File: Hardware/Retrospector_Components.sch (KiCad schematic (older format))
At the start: 134 parts, among them J1 SWD_Header, J2 Eurorack_10_pin_power, J3 Conn_01x08_Male, J4 Conn_01x08_Male, J5 Conn_01x08_Male, J6 Conn_01x08_Male, J7 USB_B_Micro, U1 STM32H743ZITx, U2 IS42S16800F-7TLI, U3 PCM5100APW, U4 SSI2164, U5 MCP6004, U6 MCP6004, U7 TL074, U8 NCV1117DT33T5G, U9 BA7807FP-E2, Y1 8MHz 20pF

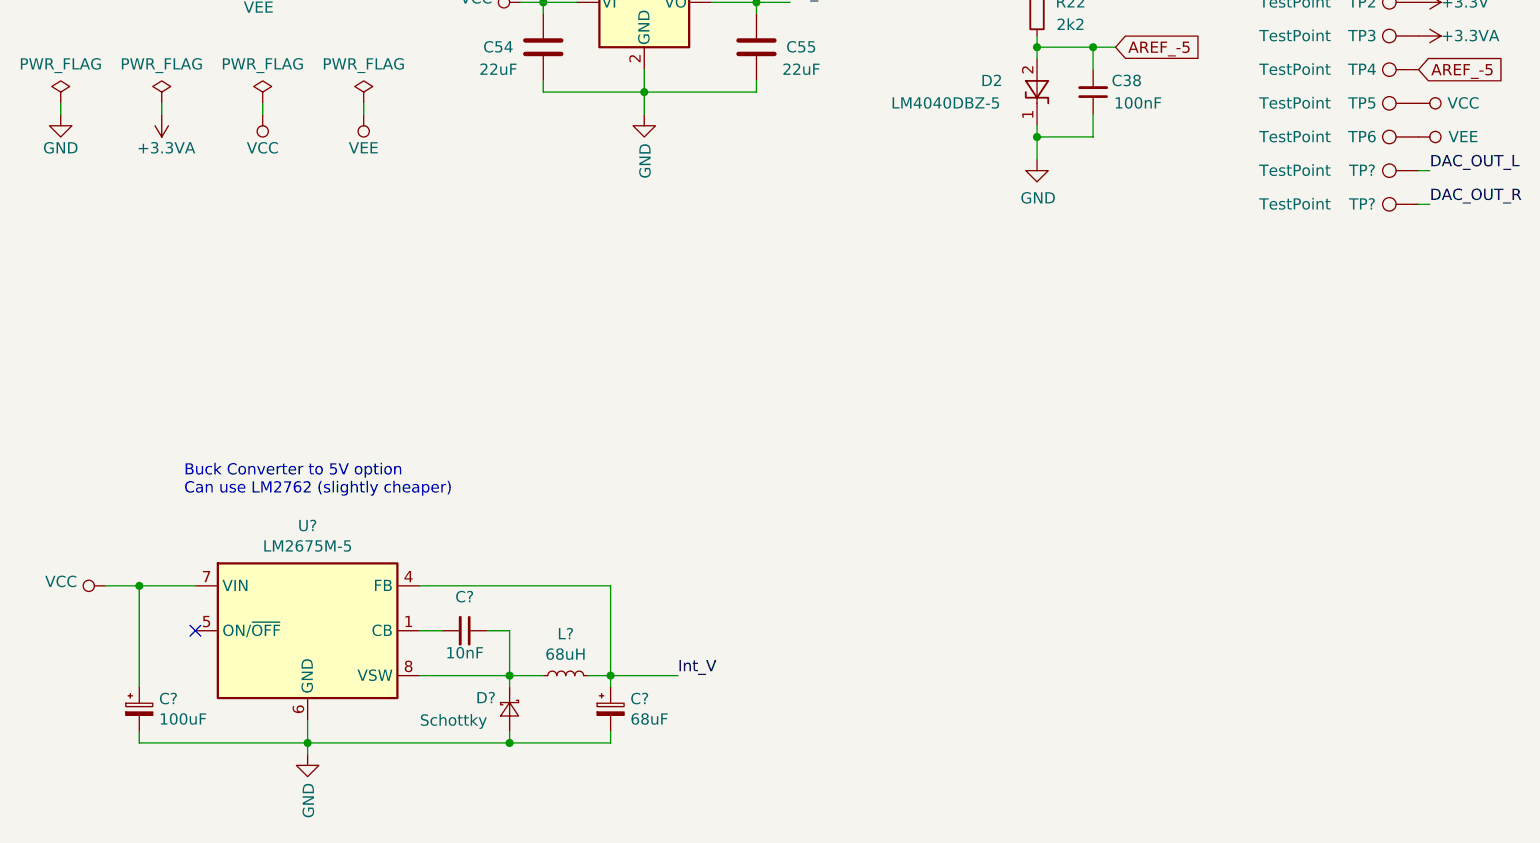
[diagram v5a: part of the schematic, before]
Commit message: Added Buck converter to PCB; other layout changes
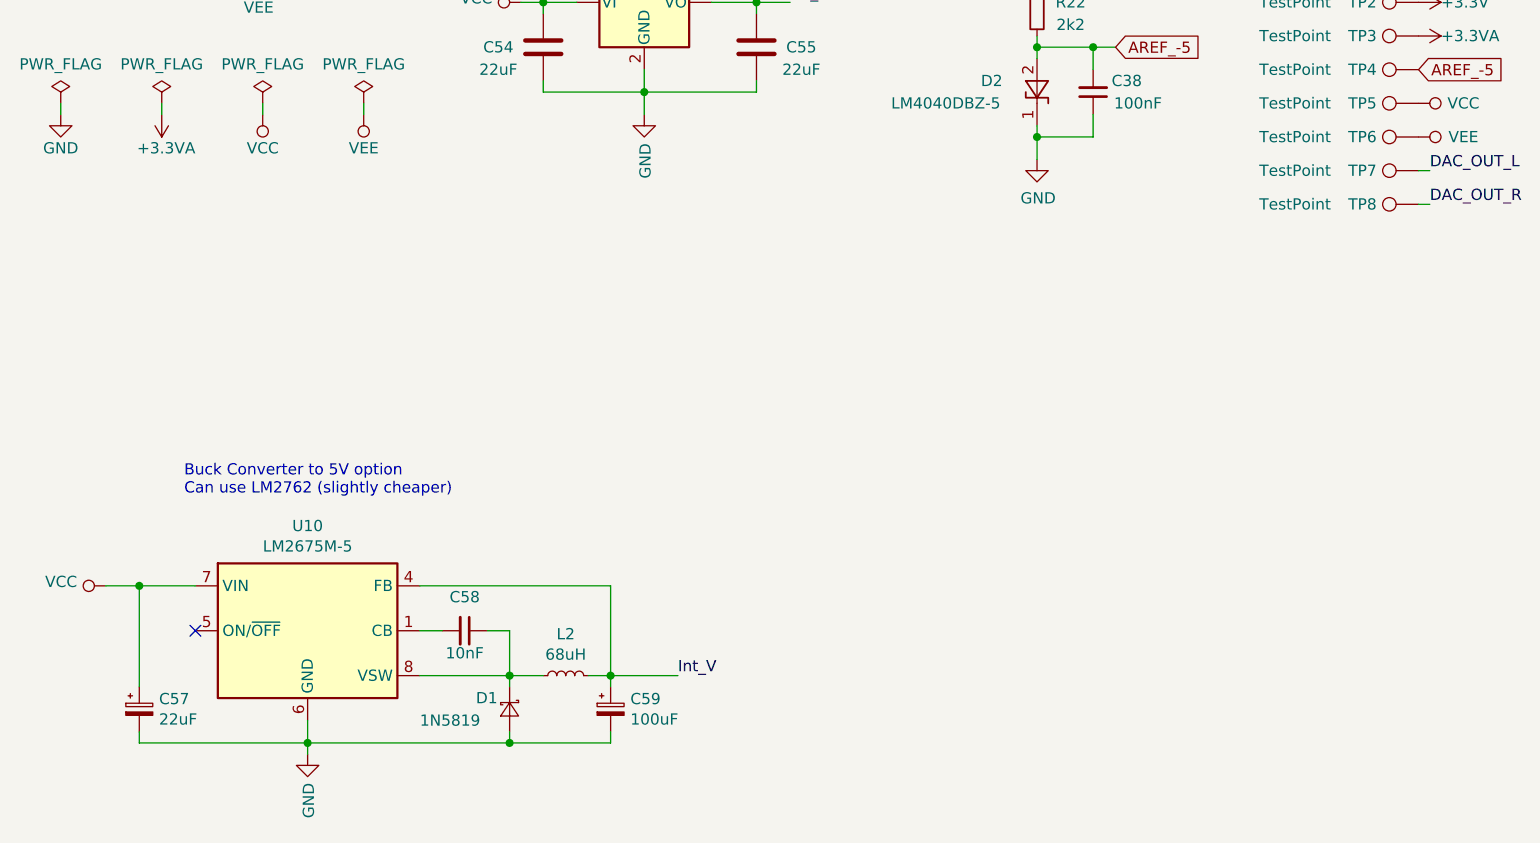
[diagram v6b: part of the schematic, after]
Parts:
- C57: renamed from C?; value 100uF -> 22uF; footprint (none) -> Capacitors_SMD:CP_Elec_4x5.8; Part_Number (none) -> C178597
- C59: renamed from C?; value 68uF -> 100uF; footprint (none) -> Capacitors_SMD:CP_Elec_6.3x5.8; Part_Number (none) -> C249982
- D1: renamed from D?; value Schottky -> 1N5819; footprint (none) -> Diodes_SMD:D_SOD-123; Part_Number (none) -> C8598
- D3, D4: Part_Number C169540 -> C8598
- L2: renamed from L?; footprint (none) -> Custom_Footprints:Inductor_SMD_6x6mm
- gave numbers to parts that had none: 4
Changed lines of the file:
@@
 F 1 "22uF" H 5000 10200 50  0000 C CNN
 F 2 "Capacitors_SMD:CP_Elec_4x5.8" H 4838 10150 50  0001 C CNN
-F 3 "~" H 4800 10300 50  0001 C CNN
+F 3 "https://datasheet.lcsc.com/szlcsc/1809131544_PANASONIC-EEEFT1V220AR_C178597.pdf" H 4800 10300 50  0001 C CNN
 F 4 "C178597" H 4800 10300 50  0001 C CNN "Part_Number"
 F 5 "" H 4800 10300 50  0001 C CNN "Rotation"
@@
 F 1 "1N5819" H 2400 10275 50  0000 C CNN
 F 2 "Diodes_SMD:D_SOD-123" H 2400 10225 50  0001 C CNN
-F 3 "http://www.vishay.com/docs/88525/1n5817.pdf" H 2400 10400 50  0001 C CNN
-F 4 "C169540" H 2400 10400 50  0001 C CNN "Part_Number"
+F 3 "https://datasheet.lcsc.com/szlcsc/Changjiang-Electronics-Tech-CJ-B5819W_C8598.pdf" H 2400 10400 50  0001 C CNN
+F 4 "C8598" H 2400 10400 50  0001 C CNN "Part_Number"
 	1    2400 10400
 	-1   0    0    1
@@
 F 1 "1N5819" H 2400 10925 50  0000 C CNN
 F 2 "Diodes_SMD:D_SOD-123" H 2400 10625 50  0001 C CNN
-F 3 "http://www.vishay.com/docs/88525/1n5817.pdf" H 2400 10800 50  0001 C CNN
-F 4 "C169540" H 2400 10800 50  0001 C CNN "Part_Number"
+F 3 "https://datasheet.lcsc.com/szlcsc/Changjiang-Electronics-Tech-CJ-B5819W_C8598.pdf" H 2400 10800 50  0001 C CNN
+F 4 "C8598" H 2400 10800 50  0001 C CNN "Part_Number"
 	1    2400 10800
 	1    0    0    -1
@@
 F 1 "22uF" V 1786 9900 50  0000 C CNN
 F 2 "Capacitors_SMD:CP_Elec_4x5.8" H 1988 9750 50  0001 C CNN
-F 3 "~" H 1950 9900 50  0001 C CNN
+F 3 "https://datasheet.lcsc.com/szlcsc/1809131544_PANASONIC-EEEFT1V220AR_C178597.pdf" H 1950 9900 50  0001 C CNN
 F 4 "C178597" H 1950 9900 50  0001 C CNN "Part_Number"
 	1    1950 9900
@@
 F 1 "22uF" V 2114 11200 50  0000 C CNN
 F 2 "Capacitors_SMD:CP_Elec_4x5.8" H 1988 11050 50  0001 C CNN
-F 3 "~" H 1950 11200 50  0001 C CNN
+F 3 "https://datasheet.lcsc.com/szlcsc/1809131544_PANASONIC-EEEFT1V220AR_C178597.pdf" H 1950 11200 50  0001 C CNN
 F 4 "C178597" H 1950 11200 50  0001 C CNN "Part_Number"
 	1    1950 11200
@@
 F 1 "22uF" H 3650 10200 50  0000 C CNN
 F 2 "Capacitors_SMD:CP_Elec_4x5.8" H 3888 10150 50  0001 C CNN
-F 3 "https://lcsc.com/product-detail/Aluminum-Electrolytic-Capacitors-SMD_Lelon-VE-100M1HTR-0505_C249452.html/?href=jlc-SMT" H 3850 10300 50  0001 C CNN
+F 3 "https://datasheet.lcsc.com/szlcsc/1809131544_PANASONIC-EEEFT1V220AR_C178597.pdf" H 3850 10300 50  0001 C CNN
 F 4 "C178597" H 3850 10300 50  0001 C CNN "Part_Number"
 F 5 "" H 3850 10300 50  0001 C CNN "Rotation"
@@
 F 1 "22uF" H 5000 11450 50  0000 C CNN
 F 2 "Capacitors_SMD:CP_Elec_4x5.8" H 4838 11400 50  0001 C CNN
-F 3 "~" H 4800 11550 50  0001 C CNN
+F 3 "https://datasheet.lcsc.com/szlcsc/1809131544_PANASONIC-EEEFT1V220AR_C178597.pdf" H 4800 11550 50  0001 C CNN
 F 4 "C178597" H 4800 11550 50  0001 C CNN "Part_Number"
 F 5 "" H 4800 11550 50  0001 C CNN "Rotation"
@@
 F 1 "22uF" H 3650 11450 50  0000 C CNN
 F 2 "Capacitors_SMD:CP_Elec_4x5.8" H 3888 11400 50  0001 C CNN
-F 3 "https://lcsc.com/product-detail/Aluminum-Electrolytic-Capacitors-SMD_Lelon-VE-100M1HTR-0505_C249452.html/?href=jlc-SMT" H 3850 11550 50  0001 C CNN
+F 3 "https://datasheet.lcsc.com/szlcsc/1809131544_PANASONIC-EEEFT1V220AR_C178597.pdf" H 3850 11550 50  0001 C CNN
 F 4 "C178597" H 3850 11550 50  0001 C CNN "Part_Number"
 F 5 "" H 3850 11550 50  0001 C CNN "Rotation"
@@
 $EndComp
 $Comp
-L Connector:TestPoint TP?
+L Connector:TestPoint TP7
 U 1 1 6D82907D
 P 7750 12100
-F 0 "TP?" V 7750 12350 50  0000 C CNN
+F 0 "TP7" V 7750 12350 50  0000 C CNN
 F 1 "TestPoint" V 7750 12650 50  0000 C CNN
 F 2 "Custom_Footprints:1.3mm_Test_Point" H 7950 12100 50  0001 C CNN
@@
 $EndComp
 $Comp
-L Connector:TestPoint TP?
+L Connector:TestPoint TP8
 U 1 1 6D829087
 P 7750 12250
-F 0 "TP?" V 7750 12500 50  0000 C CNN
+F 0 "TP8" V 7750 12500 50  0000 C CNN
 F 1 "TestPoint" V 7750 12800 50  0000 C CNN
 F 2 "Custom_Footprints:1.3mm_Test_Point" H 7950 12250 50  0001 C CNN
@@
 	7750 12250 7800 12250
 $Comp
-L Regulator_Switching:LM2675M-5 U?
+L Regulator_Switching:LM2675M-5 U10
 U 1 1 6DAC0E92
 P 2800 14150
-F 0 "U?" H 2800 14617 50  0000 C CNN
+F 0 "U10" H 2800 14617 50  0000 C CNN
 F 1 "LM2675M-5" H 2800 14526 50  0000 C CNN
 F 2 "Housings_SOIC:SOIC-8_3.9x4.9mm_Pitch1.27mm" H 2850 13800 50  0001 L CIN
@@
 NoConn ~ 2300 14150
 $Comp
-L power:VCC #PWR?
+L power:VCC #PWR0118
 U 1 1 6DB2F14A
 P 1900 13950
-F 0 "#PWR?" H 1900 13800 50  0001 C CNN
+F 0 "#PWR0118" H 1900 13800 50  0001 C CNN
 F 1 "VCC" V 1918 14077 50  0000 L CNN
 F 2 "" H 1900 13950 50  0001 C CNN
@@
 $EndComp
 $Comp
-L Device:D_Schottky_Small D?
+L Device:D_Schottky_Small D1
 U 1 1 6DB2FC15
 P 3700 14500
-F 0 "D?" V 3650 14350 50  0000 L CNN
-F 1 "Schottky" V 3750 14100 50  0000 L CNN
-F 2 "" V 3700 14500 50  0001 C CNN
-F 3 "~" V 3700 14500 50  0001 C CNN
+F 0 "D1" V 3650 14350 50  0000 L CNN
+F 1 "1N5819" V 3750 14100 50  0000 L CNN
+F 2 "Diodes_SMD:D_SOD-123" V 3700 14500 50  0001 C CNN
+F 3 "https://datasheet.lcsc.com/szlcsc/Changjiang-Electronics-Tech-CJ-B5819W_C8598.pdf" V 3700 14500 50  0001 C CNN
+F 4 "C8598" H 3700 14500 50  0001 C CNN "Part_Number"
 	1    3700 14500
 	0    1    1    0
@@
 	2800 14550 2800 14650
 $Comp
-L Device:C_Small C?
+L Device:C_Small C58
 U 1 1 6DC7C12C
 P 3500 14150
-F 0 "C?" V 3350 14150 50  0000 C CNN
+F 0 "C58" V 3350 14150 50  0000 C CNN
 F 1 "10nF" V 3600 14150 50  0000 C CNN
 F 2 "Capacitors_SMD:C_0603_HandSoldering" H 3500 14150 50  0001 C CNN
@@
 Connection ~ 3700 14350
 $Comp
-L Device:CP_Small C?
+L Device:CP_Small C59
 U 1 1 6DEA7A83
 P 4150 14500
-F 0 "C?" H 4238 14546 50  0000 L CNN
-F 1 "68uF" H 4238 14455 50  0000 L CNN
-F 2 "" H 4150 14500 50  0001 C CNN
-F 3 "~" H 4150 14500 50  0001 C CNN
+F 0 "C59" H 4238 14546 50  0000 L CNN
+F 1 "100uF" H 4238 14455 50  0000 L CNN
+F 2 "Capacitors_SMD:CP_Elec_6.3x5.8" H 4150 14500 50  0001 C CNN
+F 3 "https://datasheet.lcsc.com/szlcsc/1811201537_Lelon-VZT101M1V0606-TRO_C249982.pdf" H 4150 14500 50  0001 C CNN
+F 4 "C249982" H 4150 14500 50  0001 C CNN "Part_Number"
 	1    4150 14500
 	1    0    0    -1
@@
 	2800 14700 2800 14650
 $Comp
-L power:GND #PWR?
+L power:GND #PWR0125
 U 1 1 6DB2F5C6
 P 2800 14700
-F 0 "#PWR?" H 2800 14450 50  0001 C CNN
+F 0 "#PWR0125" H 2800 14450 50  0001 C CNN
 F 1 "GND" V 2805 14572 50  0000 R CNN
 F 2 "" H 2800 14700 50  0001 C CNN
@@
 Int_V
 $Comp
-L Device:CP_Small C?
+L Device:CP_Small C57
 U 1 1 6E46AC0A
 P 2050 14500
-F 0 "C?" H 2138 14546 50  0000 L CNN
-F 1 "100uF" H 2138 14455 50  0000 L CNN
-F 2 "" H 2050 14500 50  0001 C CNN
-F 3 "~" H 2050 14500 50  0001 C CNN
+F 0 "C57" H 2138 14546 50  0000 L CNN
+F 1 "22uF" H 2138 14455 50  0000 L CNN
+F 2 "Capacitors_SMD:CP_Elec_4x5.8" H 2050 14500 50  0001 C CNN
+F 3 "https://datasheet.lcsc.com/szlcsc/1809131544_PANASONIC-EEEFT1V220AR_C178597.pdf" H 2050 14500 50  0001 C CNN
+F 4 "C178597" H 2050 14500 50  0001 C CNN "Part_Number"
 	1    2050 14500
 	1    0    0    -1
@@
 Buck Converter to 5V option\nCan use LM2762 (slightly cheaper)
 $Comp
-L Device:L_Small L?
+L Device:L_Small L2
 U 1 1 6DEA5F2E
 P 3950 14350
-F 0 "L?" V 4135 14350 50  0000 C CNN
+F 0 "L2" V 4135 14350 50  0000 C CNN
 F 1 "68uH" V 4044 14350 50  0000 C CNN
-F 2 "" H 3950 14350 50  0001 C CNN
+F 2 "Custom_Footprints:Inductor_SMD_6x6mm" H 3950 14350 50  0001 C CNN
 F 3 "https://datasheet.lcsc.com/szlcsc/1912111437_3L-COILS-SNR6045K-680M_C326343.pdf" H 3950 14350 50  0001 C CNN
 F 4 "C326343" V 3950 14350 50  0001 C CNN "Part_Number"

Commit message: Completed draft of rev 2 pcb
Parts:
- removed C55: 22uF, Capacitors_SMD:CP_Elec_4x5.8, symbol Device:C
- C36, C41, C54: symbol Device:C -> Device:CP_Small
- TP7, TP8: footprint Custom_Footprints:1.3mm_Test_Point -> Measurement_Points:Measurement_Point_Square-SMD-Pad_Small
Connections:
- net VSW: now reaches C58.1, D1.1 (K), L2.1, U10.8 (VSW)
- net AREF_-5 renamed -5V_REF
- no-connect marks 64 -> 51
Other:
- note added: "Can use AS3364D (linerar VCA) with R43 and C56 in place;\nRemove for SSI2164"
- note added: "Optional test circuit for intermediate LDO"
- note added: "Test Points"
- note removed: "ADCs Used"
- note removed: "FIXME - resistors R42/43 are redundant??"
- note removed: "NOTE - Mode unconnected = Class AB\n7.5k to VCC = Class A (Lower THD, higher noise)"
- moved on the sheet: C13, C17, C18, C22, C23, C24, C27, C28, C31, C33, C35, C38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

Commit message: Include inverting op amp output stage so output is not polarity reversed
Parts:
- added U11: TL072, Housings_SOIC:SOIC-8_3.9x4.9mm_Pitch1.27mm, symbol Amplifier_Operational:TL072
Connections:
- net EXT_AUDIO_OUT_L: now also R21.1; no longer R20.1
- net EXT_AUDIO_OUT_R: now also R20.1; no longer R21.1
- net GND: now also U11.3 (+), U11.5 (+)
- net VCC: now also U11.8 (V+)
- net VEE: now also U11.4 (V-)
- net at C51.1, R18.1, U7.8: now also R21.2, U11.1, U11.2 (-); no longer R20.2
- net at C52.1, R19.1, U7.14: now also R20.2, U11.6 (-), U11.7; no longer R21.2
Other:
- note added: "DAC and VCA"
- note added: "Output Mixers and Inverting Buffers"
- note removed: "DAC and VCAs"
- note removed: "Output Buffers"
- moved on the sheet: C13, C17, C22, C24, C29, C30, C31, C32, C33, C34, C35, C38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
